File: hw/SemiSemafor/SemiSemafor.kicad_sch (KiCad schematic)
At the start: 40 parts, among them J1 USB_PCB, J2 ESP-Programing_conector, SW1 SW_DIP_x01, SW2 SW_DIP_x01, U1 LD39200, U2 ESP32-C3-MINI-1

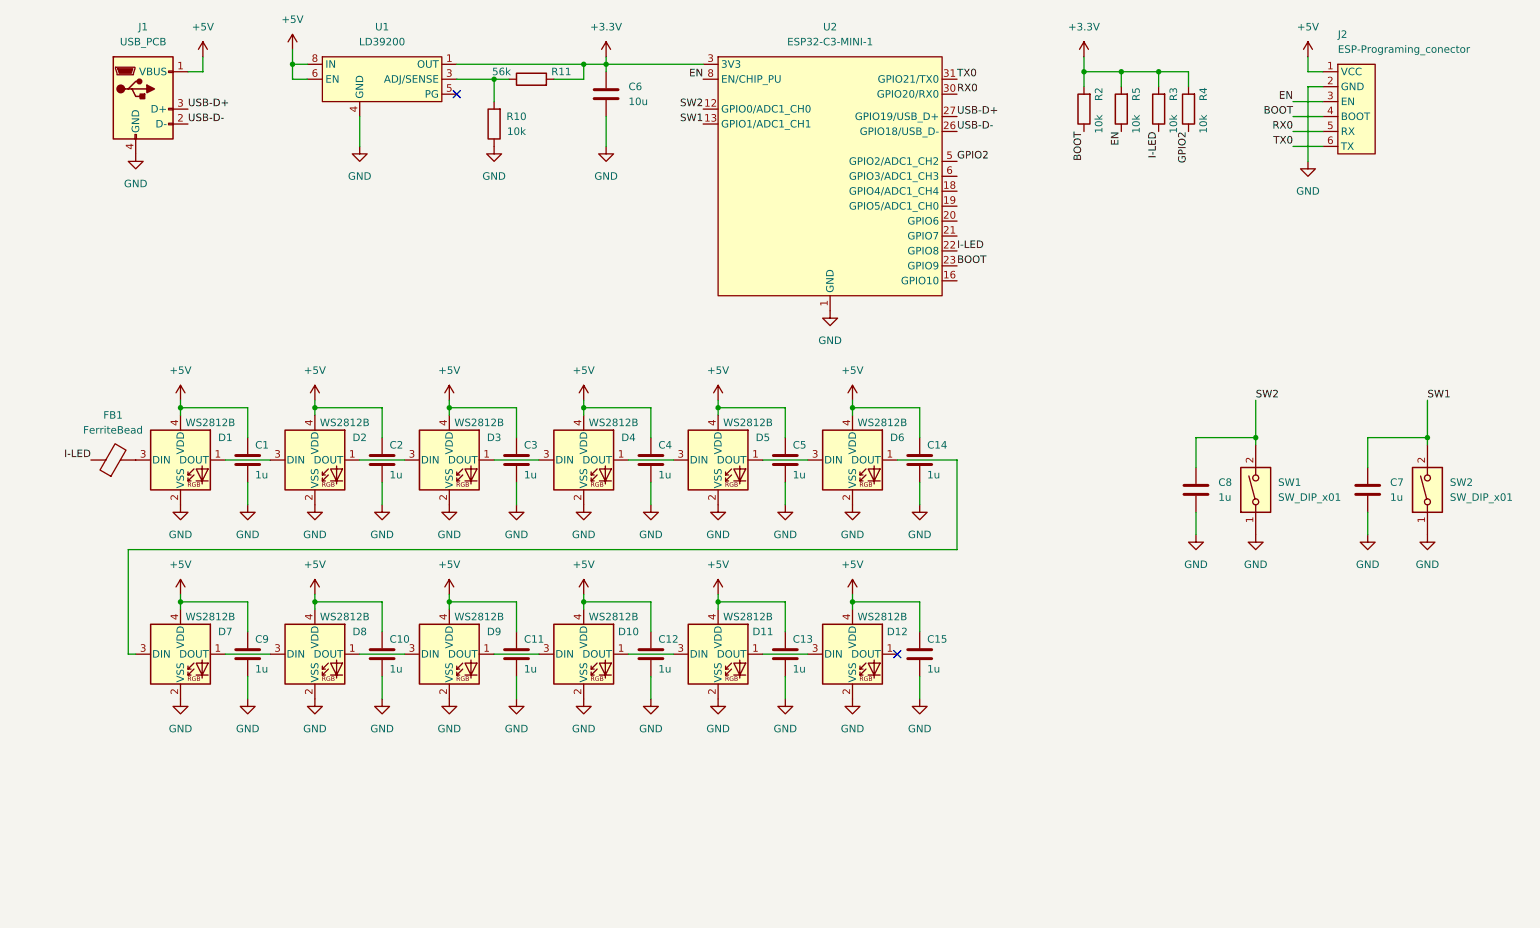
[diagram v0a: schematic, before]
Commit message: Add accelerometer
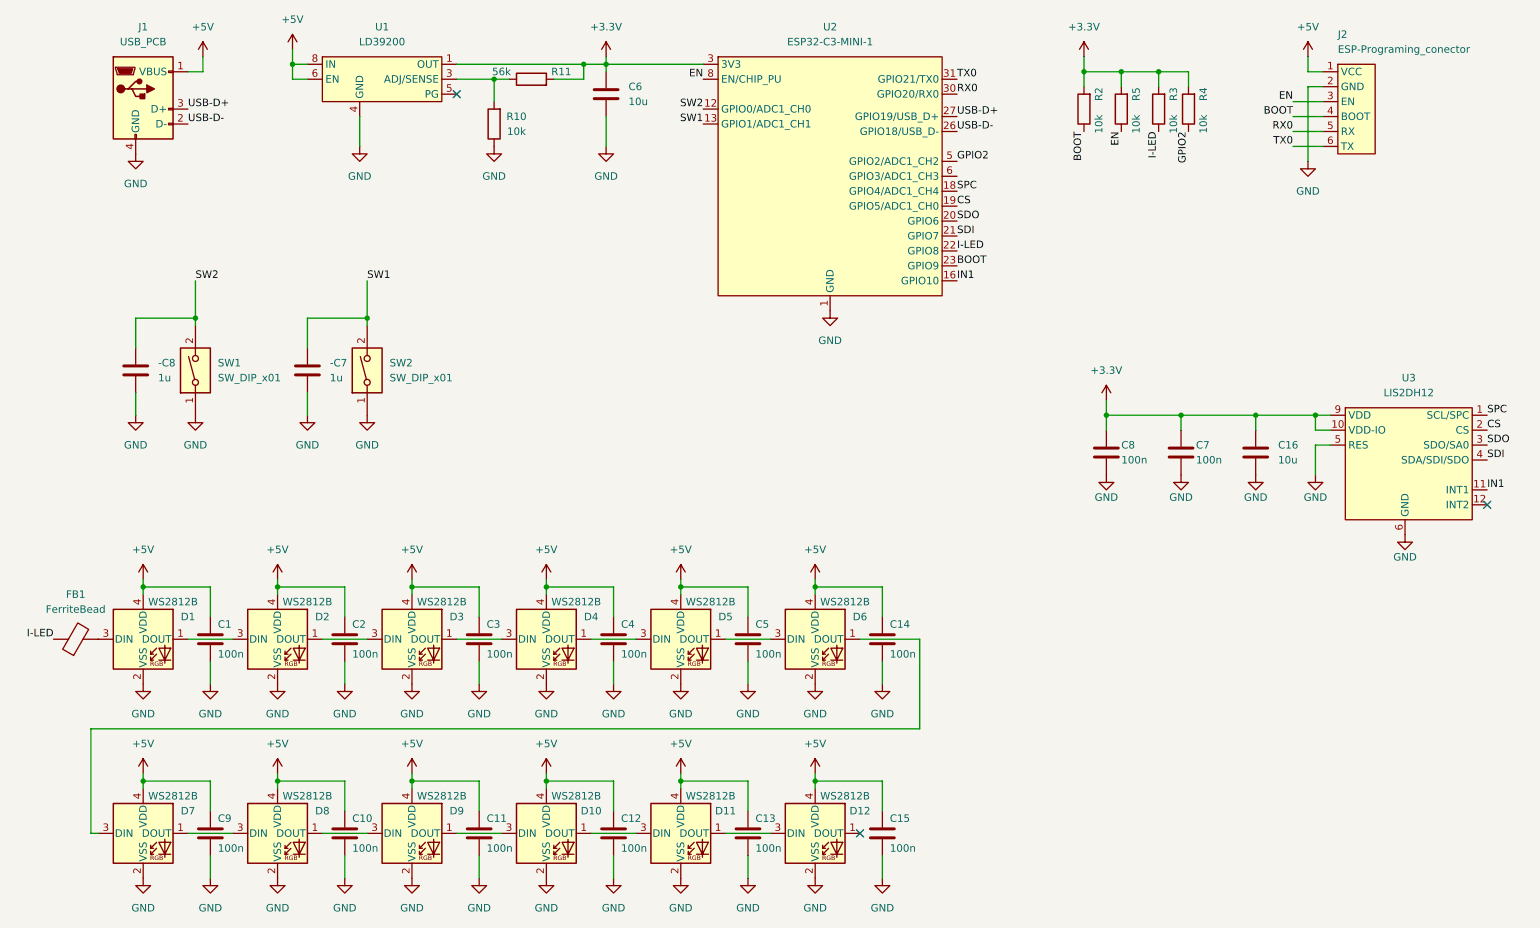
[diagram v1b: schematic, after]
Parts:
- added C16: 10u, Capacitor_SMD:C_0603_1608Metric, symbol Device:C
- added C7, C8: 100n, Capacitor_SMD:C_0402_1005Metric, symbol Device:C
- added U3: LIS2DH12, Package_LGA:LGA-12_2x2mm_P0.5mm, symbol RKL-MEMS:LIS2DH12
- C1, C10, C11, C12, C13, C14, C15, C2, C3, C4, C5, C9: value 1u -> 100n; LCSC C52923 -> C1525
- renumbered C7 to -C7, C8 to -C8
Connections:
- net +3.3V: now also C16.1, C7.1, C8.1, U3.10 (VDD-IO), U3.9 (VDD)
- net GND: now also C16.2, C7.2, C8.2, U3.5 (RES), U3.6 (GND), U3.7 (GND), U3.8 (GND)
- net IN1: now reaches U2.16 (GPIO10)
- net IN1: now also U3.11 (INT1)
- net SPC: now reaches U2.18 (GPIO4/ADC1_CH4)
- net SPC: now also U3.1 (SCL/SPC)
- net CS: now reaches U2.19 (GPIO5/ADC1_CH0)
- net CS: now also U3.2 (CS)
- net SDO: now reaches U2.20 (GPIO6)
- net SDO: now also U3.3 (SDO/SA0)
- net SDI: now reaches U2.21 (GPIO7)
- net SDI: now also U3.4 (SDA/SDI/SDO)
- no-connect marks 2 -> 3
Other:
- moved on the sheet: -C7, -C8, C1, C10, C11, C12, C13, C14, C15, C2, C3, C4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

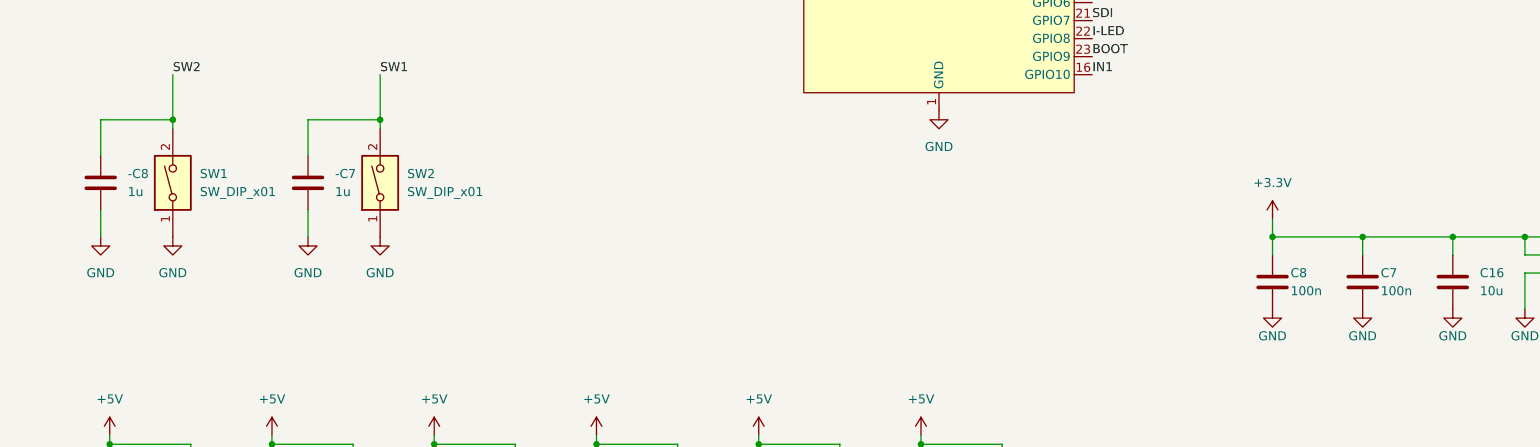
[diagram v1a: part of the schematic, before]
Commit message: Add accelerometer on PCB
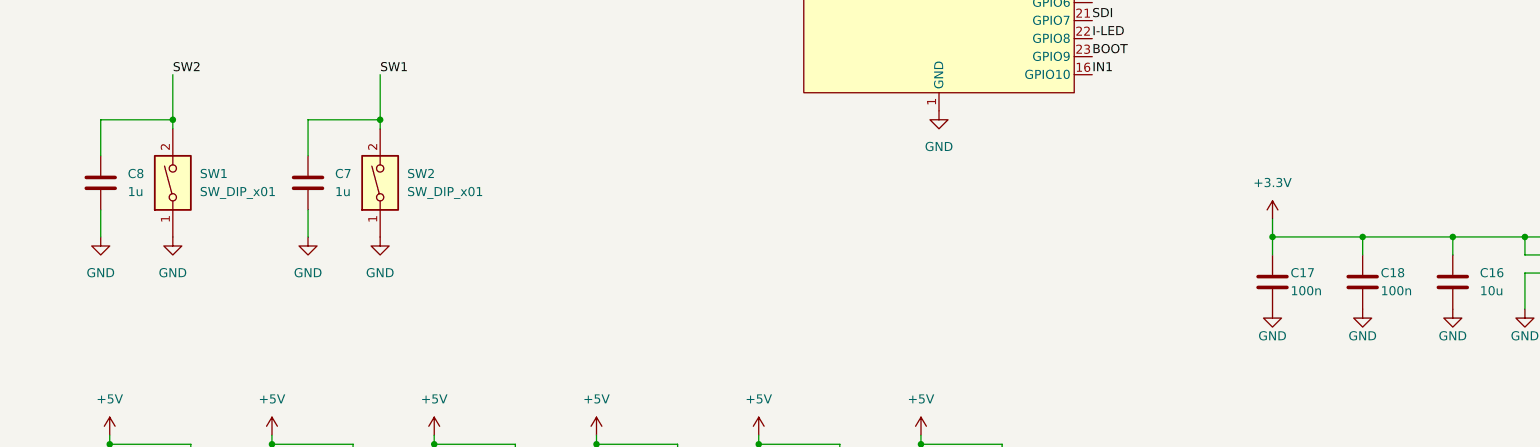
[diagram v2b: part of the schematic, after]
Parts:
- removed C7, C8: 100n, Capacitor_SMD:C_0402_1005Metric, symbol Device:C
- added C17, C18: 100n, Capacitor_SMD:C_0402_1005Metric, symbol Device:C
- renumbered -C7 to C7, -C8 to C8
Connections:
- net +3.3V: now also C17.1, C18.1
- net GND: now also C17.2, C18.2
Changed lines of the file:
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@@
   (symbol (lib_id "Device:C") (at 67.31 99.06 0) (unit 1)
     (in_bom yes) (on_board yes) (dnp no) (fields_autoplaced)
-    (property "Reference" "-C7" (at 71.12 97.7899 0)
+    (property "Reference" "C7" (at 71.12 97.7899 0)
       (effects (font (size 1.27 1.27)) (justify left))
     )
@@
       (project "SemiSemafor"
         (path "/fb82d987-26cf-425e-8e99-22ecb59c8a96"
-          (reference "-C7") (unit 1)
+          (reference "C7") (unit 1)
         )
       )
@@
     )
   )
-  (symbol (lib_id "Device:C") (at 203.2 113.03 0) (unit 1)
-    (in_bom yes) (on_board yes) (dnp no)
-    (property "Reference" "C8" (at 205.74 111.76 0)
-      (effects (font (size 1.27 1.27)) (justify left))
-    )
-    (property "Value" "100n" (at 205.74 114.3 0)
-      (effects (font (size 1.27 1.27)) (justify left))
-    )
-    (property "Footprint" "Capacitor_SMD:C_0402_1005Metric" (at 204.1652 116.84 0)
-      (effects (font (size 1.27 1.27)) hide)
-    )
-    (property "Datasheet" "~" (at 203.2 113.03 0)
-      (effects (font (size 1.27 1.27)) hide)
-    )
-    (property "LCSC" "C1525" (at 203.2 113.03 0)
-      (effects (font (size 1.27 1.27)) hide)
-    )
-    (pin "1")
-    (pin "2")
-    (instances
-      (project "SemiSemafor"
-        (path "/fb82d987-26cf-425e-8e99-22ecb59c8a96"
-          (reference "C8") (unit 1)
-        )
-      )
-    )
-  )
   (symbol (lib_id "power:+5V") (at 85.09 134.62 0) (mirror y) (unit 1)
     (in_bom yes) (on_board yes) (dnp no) (fields_autoplaced)
@@
         (path "/fb82d987-26cf-425e-8e99-22ecb59c8a96"
           (reference "D2") (unit 1)
+        )
+      )
+    )
+  )
+  (symbol (lib_id "Device:C") (at 203.2 113.03 0) (unit 1)
+    (in_bom yes) (on_board yes) (dnp no)
+    (property "Reference" "C17" (at 205.74 111.76 0)
+      (effects (font (size 1.27 1.27)) (justify left))
+    )
+    (property "Value" "100n" (at 205.74 114.3 0)
+      (effects (font (size 1.27 1.27)) (justify left))
+    )
+    (property "Footprint" "Capacitor_SMD:C_0402_1005Metric" (at 204.1652 116.84 0)
+      (effects (font (size 1.27 1.27)) hide)
+    )
+    (property "Datasheet" "~" (at 203.2 113.03 0)
+      (effects (font (size 1.27 1.27)) hide)
+    )
+    (property "LCSC" "C1525" (at 203.2 113.03 0)
+      (effects (font (size 1.27 1.27)) hide)
+    )
+    (pin "1")
+    (pin "2")
+    (instances
+      (project "SemiSemafor"
+        (path "/fb82d987-26cf-425e-8e99-22ecb59c8a96"
+          (reference "C17") (unit 1)
         )
       )
@@
   (symbol (lib_id "Device:C") (at 38.1 99.06 0) (unit 1)
     (in_bom yes) (on_board yes) (dnp no) (fields_autoplaced)
-    (property "Reference" "-C8" (at 41.91 97.7899 0)
+    (property "Reference" "C8" (at 41.91 97.7899 0)
       (effects (font (size 1.27 1.27)) (justify left))
     )
@@
       (project "SemiSemafor"
         (path "/fb82d987-26cf-425e-8e99-22ecb59c8a96"
-          (reference "-C8") (unit 1)
+          (reference "C8") (unit 1)
         )
       )
@@
     )
   )
+  (symbol (lib_id "Device:C") (at 215.9 113.03 0) (unit 1)
+    (in_bom yes) (on_board yes) (dnp no)
+    (property "Reference" "C18" (at 218.44 111.76 0)
+      (effects (font (size 1.27 1.27)) (justify left))
+    )
+    (property "Value" "100n" (at 218.44 114.3 0)
+      (effects (font (size 1.27 1.27)) (justify left))
+    )
+    (property "Footprint" "Capacitor_SMD:C_0402_1005Metric" (at 216.8652 116.84 0)
+      (effects (font (size 1.27 1.27)) hide)
+    )
+    (property "Datasheet" "~" (at 215.9 113.03 0)
+      (effects (font (size 1.27 1.27)) hide)
+    )
+    (property "LCSC" "C1525" (at 215.9 113.03 0)
+      (effects (font (size 1.27 1.27)) hide)
+    )
+    (pin "1")
+    (pin "2")
+    (instances
+      (project "SemiSemafor"
+        (path "/fb82d987-26cf-425e-8e99-22ecb59c8a96"
+          (reference "C18") (unit 1)
+        )
+      )
+    )
+  )
   (symbol (lib_id "Switch:SW_DIP_x01") (at 77.47 99.06 90) (unit 1)
     (in_bom yes) (on_board yes) (dnp no) (fields_autoplaced)
@@
         (path "/fb82d987-26cf-425e-8e99-22ecb59c8a96"
           (reference "D5") (unit 1)
-        )
-      )
-    )
-  )
-  (symbol (lib_id "Device:C") (at 215.9 113.03 0) (unit 1)
-    (in_bom yes) (on_board yes) (dnp no)
-    (property "Reference" "C7" (at 218.44 111.76 0)
-      (effects (font (size 1.27 1.27)) (justify left))
-    )
-    (property "Value" "100n" (at 218.44 114.3 0)
-      (effects (font (size 1.27 1.27)) (justify left))
-    )
-    (property "Footprint" "Capacitor_SMD:C_0402_1005Metric" (at 216.8652 116.84 0)
-      (effects (font (size 1.27 1.27)) hide)
-    )
-    (property "Datasheet" "~" (at 215.9 113.03 0)
-      (effects (font (size 1.27 1.27)) hide)
-    )
-    (property "LCSC" "C1525" (at 215.9 113.03 0)
-      (effects (font (size 1.27 1.27)) hide)
-    )
-    (pin "1")
-    (pin "2")
-    (instances
-      (project "SemiSemafor"
-        (path "/fb82d987-26cf-425e-8e99-22ecb59c8a96"
-          (reference "C7") (unit 1)
         )
       )
@@
   )
   (symbol (lib_id "RKL-MEMS:LIS2DH12") (at 254 106.68 0) (unit 1)
-    (in_bom yes) (on_board yes) (dnp no) (fields_autoplaced)
+    (in_bom yes) (on_board yes) (dnp no)
     (property "Reference" "U3" (at 254.635 100.33 0)
       (effects (font (size 1.27 1.27)))

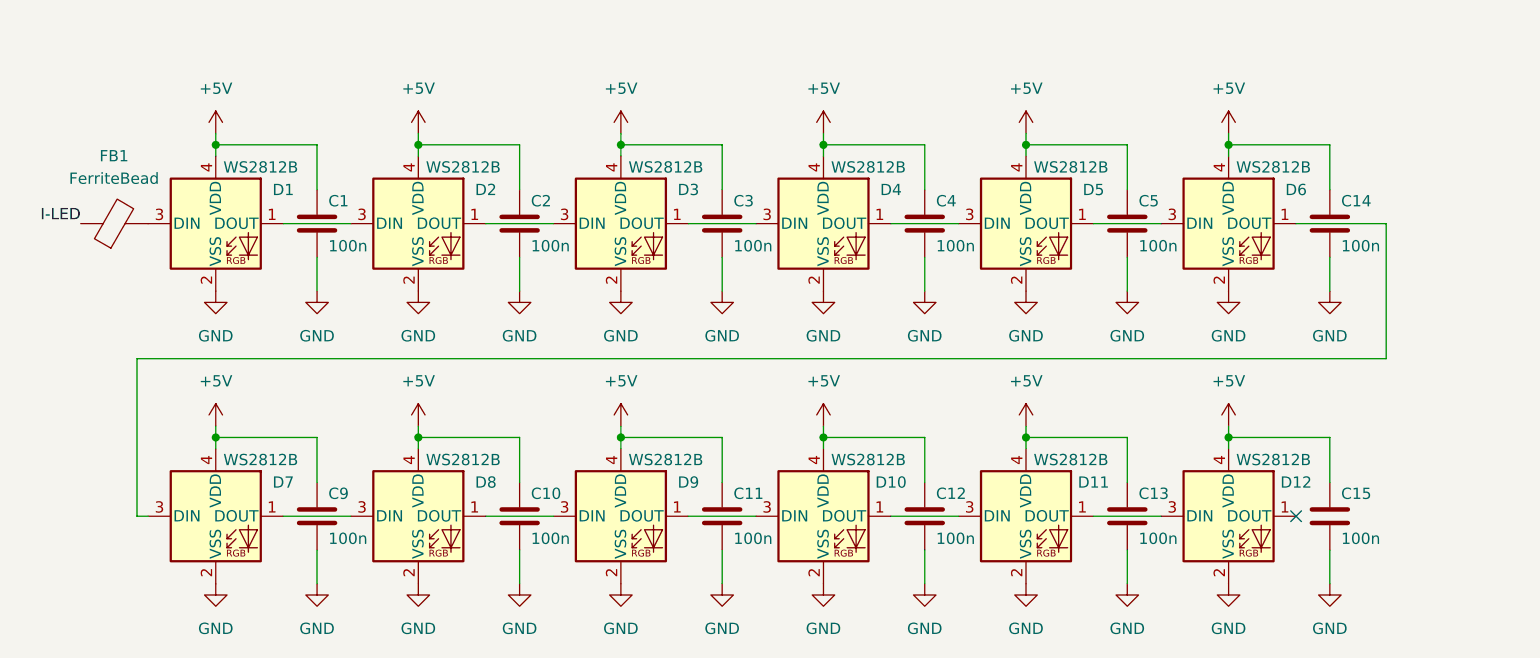
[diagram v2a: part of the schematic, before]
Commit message: 5mm LED
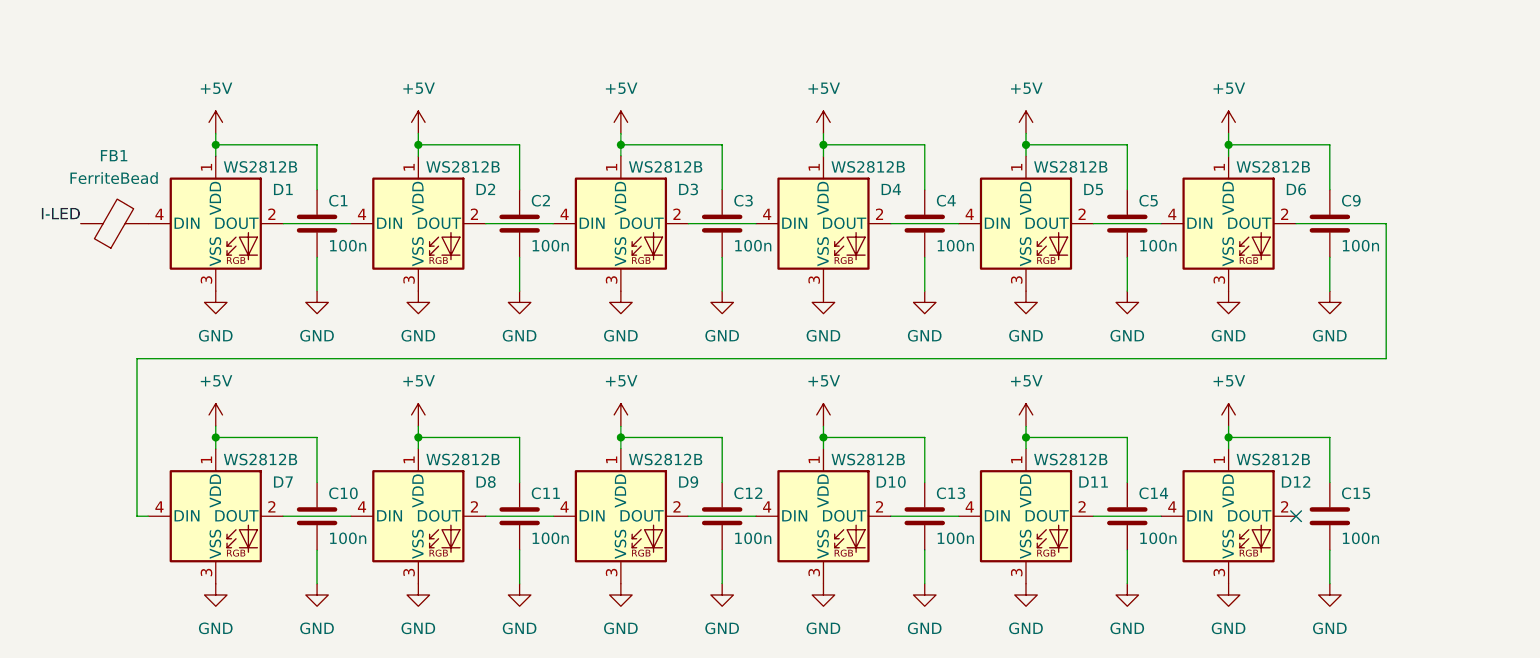
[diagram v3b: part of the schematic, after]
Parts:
- C1, C10, C11, C12, C13, C14, C15, C2, C3, C4, C5, C9: footprint Capacitor_SMD:C_0402_1005Metric -> Capacitor_SMD:C_0603_1608Metric; LCSC C1525 -> C14663
- D1, D10, D11, D12, D2, D3, D4, D5, D6, D7, D8, D9: footprint LED_SMD:LED_WS2812B-2020_PLCC4_2.0x2.0mm -> LED_SMD:LED_WS2812B_PLCC4_5.0x5.0mm_P3.2mm; LCSC C965555 -> C2920042
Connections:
- net +5V: now also D1.1 (VDD), D10.1 (VDD), D11.1 (VDD), D12.1 (VDD), D2.1 (VDD), D3.1 (VDD), D4.1 (VDD), D5.1 (VDD), D6.1 (VDD), D7.1 (VDD), D8.1 (VDD), D9.1 (VDD); no longer D1.4 (VDD), D10.4 (VDD), D11.4 (VDD), D12.4 (VDD), D2.4 (VDD), D3.4 (VDD), D4.4 (VDD), D5.4 (VDD), D6.4 (VDD), D7.4 (VDD), D8.4 (VDD), D9.4 (VDD)
- net GND: now also D1.3 (VSS), D10.3 (VSS), D11.3 (VSS), D12.3 (VSS), D2.3 (VSS), D3.3 (VSS), D4.3 (VSS), D5.3 (VSS), D6.3 (VSS), D7.3 (VSS), D8.3 (VSS), D9.3 (VSS); no longer D1.2 (VSS), D10.2 (VSS), D11.2 (VSS), D12.2 (VSS), D2.2 (VSS), D3.2 (VSS), D4.2 (VSS), D5.2 (VSS), D6.2 (VSS), D7.2 (VSS), D8.2 (VSS), D9.2 (VSS)
- net at FB1.2: now also D1.4 (DIN); no longer D1.3 (DIN)
- new net: D2.2 (DOUT), D3.4 (DIN)
- new net: D1.2 (DOUT), D2.4 (DIN)
- new net: D6.2 (DOUT), D7.4 (DIN)
- new net: D5.2 (DOUT), D6.4 (DIN)
- new net: D11.2 (DOUT), D12.4 (DIN)
- new net: D10.2 (DOUT), D11.4 (DIN)
- new net: D10.4 (DIN), D9.2 (DOUT)
- new net: D3.2 (DOUT), D4.4 (DIN)
- new net: D8.2 (DOUT), D9.4 (DIN)
- new net: D7.2 (DOUT), D8.4 (DIN)
- new net: D4.2 (DOUT), D5.4 (DIN)

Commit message: v2.1.0
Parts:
- added J3: Conn_01x02, RKL-ESP:ESP-Small-programming connector, symbol Connector_Generic:Conn_01x02
- U2: JLCPCB_CORRECTION (none) -> 0;0;180
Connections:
- net BOOT: now also J3.2 (Pin_2)
- net EN: now also J3.1 (Pin_1)
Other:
- moved on the sheet: J2, R2, R3, R4, R5

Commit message: Change package of FB1
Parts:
- FB1: footprint Inductor_SMD:L_0201_0603Metric -> Inductor_SMD:L_0402_1005Metric; LCSC C160965 -> C275411
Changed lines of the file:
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@@
       (effects (font (size 1.27 1.27)))
     )
-    (property "Footprint" "Inductor_SMD:L_0201_0603Metric" (at 27.94 146.558 90)
+    (property "Footprint" "Inductor_SMD:L_0402_1005Metric" (at 27.94 146.558 90)
       (effects (font (size 1.27 1.27)) hide)
     )
@@
       (effects (font (size 1.27 1.27)) hide)
     )
-    (property "LCSC" "C160965" (at 27.94 144.78 90)
+    (property "LCSC" "C275411" (at 27.94 144.78 90)
       (effects (font (size 1.27 1.27)) hide)
     )

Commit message: evert "Change package of FB1"
This reverts commit 3fec99b397d1e8d7d4d9ec397064b3177b82c20d.

# Conflicts:
#	hw/SemiSemafor/SemiSemafor.kicad_pcb
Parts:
- FB1: footprint Inductor_SMD:L_0402_1005Metric -> Inductor_SMD:L_0201_0603Metric; LCSC C275411 -> C160965
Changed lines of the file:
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@@
       (effects (font (size 1.27 1.27)))
     )
-    (property "Footprint" "Inductor_SMD:L_0402_1005Metric" (at 27.94 146.558 90)
+    (property "Footprint" "Inductor_SMD:L_0201_0603Metric" (at 27.94 146.558 90)
       (effects (font (size 1.27 1.27)) hide)
     )
@@
       (effects (font (size 1.27 1.27)) hide)
     )
-    (property "LCSC" "C275411" (at 27.94 144.78 90)
+    (property "LCSC" "C160965" (at 27.94 144.78 90)
       (effects (font (size 1.27 1.27)) hide)
     )
